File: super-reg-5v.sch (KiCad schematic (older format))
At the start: 41 parts, among them Q1 2SA1015, Q2 D44H11, U1 LM317T, U2 AD825, U3 AD825, X1 AC_IN, X2 DC_OUT

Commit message: migrate library
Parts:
- LED1: symbol LED -> LED-RESCUE-super-reg-5v
- U2, U3: symbol TL081 -> TL081-RESCUE-super-reg-5v
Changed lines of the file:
@@
 EESchema Schematic File Version 2
+LIBS:super-reg-5v-rescue
 LIBS:power
 LIBS:device
@@
 $EndComp
 $Comp
-L LED LED1
+L LED-RESCUE-super-reg-5v LED1
 U 1 1 57943EDE
 P 4700 3050
@@
 $EndComp
 $Comp
-L TL081 U2
+L TL081-RESCUE-super-reg-5v U2
 U 1 1 5794409D
 P 6900 3600
@@
 	3750 2350 4000 2350
 $Comp
-L TL081 U3
+L TL081-RESCUE-super-reg-5v U3
 U 1 1 57C2A197
 P 6900 4900

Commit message: update components
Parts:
- D3: symbol ZENER -> D_Zener
- JP1: symbol JUMPER3 -> Jumper_NC_Dual
- U2, U3: symbol TL081-RESCUE-super-reg-5v -> TL071
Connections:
- no-connect marks 0 -> 4
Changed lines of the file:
@@
 EESchema Schematic File Version 2
-LIBS:super-reg-5v-rescue
 LIBS:power
 LIBS:device
@@
 LIBS:DB-1
 LIBS:semi-trans-OnSemi
-LIBS:super-reg-5v-cache
 EELAYER 25 0
 EELAYER END
@@
 $EndComp
 $Comp
-L TL081-RESCUE-super-reg-5v U2
+L TL071 U2
 U 1 1 5794409D
 P 6900 3600
@@
 $EndComp
 $Comp
-L ZENER D3
+L D_Zener D3
 U 1 1 579441EA
 P 5800 3600
@@
 $EndComp
 $Comp
-L JUMPER3 JP1
+L Jumper_NC_Dual JP1
 U 1 1 5794546A
 P 6500 2450
@@
 	5100 3250 5100 3200
 Wire Wire Line
-	6000 3600 6050 3600
+	5950 3600 6050 3600
 Wire Wire Line
 	6350 3600 6600 3600
@@
 	5500 2850 5500 3900
 Wire Wire Line
-	5600 3600 5500 3600
+	5500 3600 5650 3600
 Connection ~ 5500 3600
 Wire Wire Line
@@
 	3750 2350 4000 2350
 $Comp
-L TL081-RESCUE-super-reg-5v U3
+L TL071 U3
 U 1 1 57C2A197
 P 6900 4900
@@
 	2950 5200 2400 5200
 Connection ~ 2400 5200
+NoConn ~ 6900 5200
+NoConn ~ 6800 5200
+NoConn ~ 6800 3900
+NoConn ~ 6900 3900
+$Comp
+L PWR_FLAG #PWR07
+U 1 1 591C8082
+P 6500 3000
+F 0 "#PWR07" H 6500 3000 50  0001 C CNN
+F 1 "PWR_FLAG" H 6500 3000 50  0001 C CNN
+F 2 "" H 6500 3000 60  0000 C CNN
+F 3 "" H 6500 3000 60  0000 C CNN
+	1    6500 3000
+	1    0    0    -1
+$EndComp
 $EndSCHEMATC

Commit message: fix library error
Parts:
- LED1: symbol LED-RESCUE-super-reg-5v -> LED
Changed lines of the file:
@@
 LIBS:DB-1
 LIBS:semi-trans-OnSemi
+LIBS:super-reg-5v-cache
 EELAYER 25 0
 EELAYER END
@@
 $EndComp
 $Comp
-L LED-RESCUE-super-reg-5v LED1
+L LED LED1
 U 1 1 57943EDE
 P 4700 3050
@@
 	6350 3600 6600 3600
 Wire Wire Line
-	4700 2700 4700 2850
+	4700 2700 4700 2900
 Wire Wire Line
 	4000 2700 5400 2700
@@
 	4800 3450 4700 3450
 Wire Wire Line
-	4700 3250 4700 3600
+	4700 3200 4700 3600
 Connection ~ 4700 3450
 Wire Wire Line

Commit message: update footprints
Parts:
- C11, C8: footprint Capacitors_ThroughHole:C_Radial_D8_L13_P3.8 -> Capacitors_ThroughHole:CP_Radial_D8.0mm_P3.80mm
- C3, C5, C6, C9: footprint Capacitors_ThroughHole:C_Radial_D6.3_L11.2_P2.5 -> Capacitors_ThroughHole:CP_Radial_D6.3mm_P2.50mm
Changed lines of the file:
@@
 F 0 "C3" H 4275 3550 50  0000 L CNN
 F 1 "100u 35v LowESR" H 4250 3650 50  0000 L CNN
-F 2 "Capacitors_ThroughHole:C_Radial_D6.3_L11.2_P2.5" H 4288 3300 50  0001 C CNN
+F 2 "Capacitors_ThroughHole:CP_Radial_D6.3mm_P2.50mm" H 4288 3300 50  0001 C CNN
 F 3 "" H 4250 3450 50  0000 C CNN
 	1    4250 3450
@@
 F 0 "C6" H 6125 2400 50  0000 L CNN
 F 1 "100u 35v LowESR" H 5350 2450 50  0000 L CNN
-F 2 "Capacitors_ThroughHole:C_Radial_D6.3_L11.2_P2.5" H 6138 2150 50  0001 C CNN
+F 2 "Capacitors_ThroughHole:CP_Radial_D6.3mm_P2.50mm" H 6138 2150 50  0001 C CNN
 F 3 "" H 6100 2300 50  0000 C CNN
 	1    6100 2300
@@
 F 0 "C5" H 5825 4000 50  0000 L CNN
 F 1 "100u LowESR" V 5650 3650 50  0000 L CNN
-F 2 "Capacitors_ThroughHole:C_Radial_D6.3_L11.2_P2.5" H 5838 3750 50  0001 C CNN
+F 2 "Capacitors_ThroughHole:CP_Radial_D6.3mm_P2.50mm" H 5838 3750 50  0001 C CNN
 F 3 "" H 5800 3900 50  0000 C CNN
 	1    5800 3900
@@
 F 0 "C8" H 7875 4050 50  0000 L CNN
 F 1 "100u EP-Cap" H 7500 3800 50  0000 L CNN
-F 2 "Capacitors_ThroughHole:C_Radial_D8_L13_P3.8" H 7888 3800 50  0001 C CNN
+F 2 "Capacitors_ThroughHole:CP_Radial_D8.0mm_P3.80mm" H 7888 3800 50  0001 C CNN
 F 3 "" H 7850 3950 50  0000 C CNN
 	1    7850 3950
@@
 F 0 "C9" H 9025 3600 50  0000 L CNN
 F 1 "100u" H 9025 3400 50  0000 L CNN
-F 2 "Capacitors_ThroughHole:C_Radial_D6.3_L11.2_P2.5" H 9038 3350 50  0001 C CNN
+F 2 "Capacitors_ThroughHole:CP_Radial_D6.3mm_P2.50mm" H 9038 3350 50  0001 C CNN
 F 3 "" H 9000 3500 50  0000 C CNN
 	1    9000 3500
@@
 F 0 "C11" H 9875 3650 50  0000 L CNN
 F 1 "220u OS-CON" H 9875 3450 50  0000 L CNN
-F 2 "Capacitors_ThroughHole:C_Radial_D8_L13_P3.8" H 9888 3400 50  0001 C CNN
+F 2 "Capacitors_ThroughHole:CP_Radial_D8.0mm_P3.80mm" H 9888 3400 50  0001 C CNN
 F 3 "" H 9850 3550 50  0000 C CNN
 	1    9850 3550

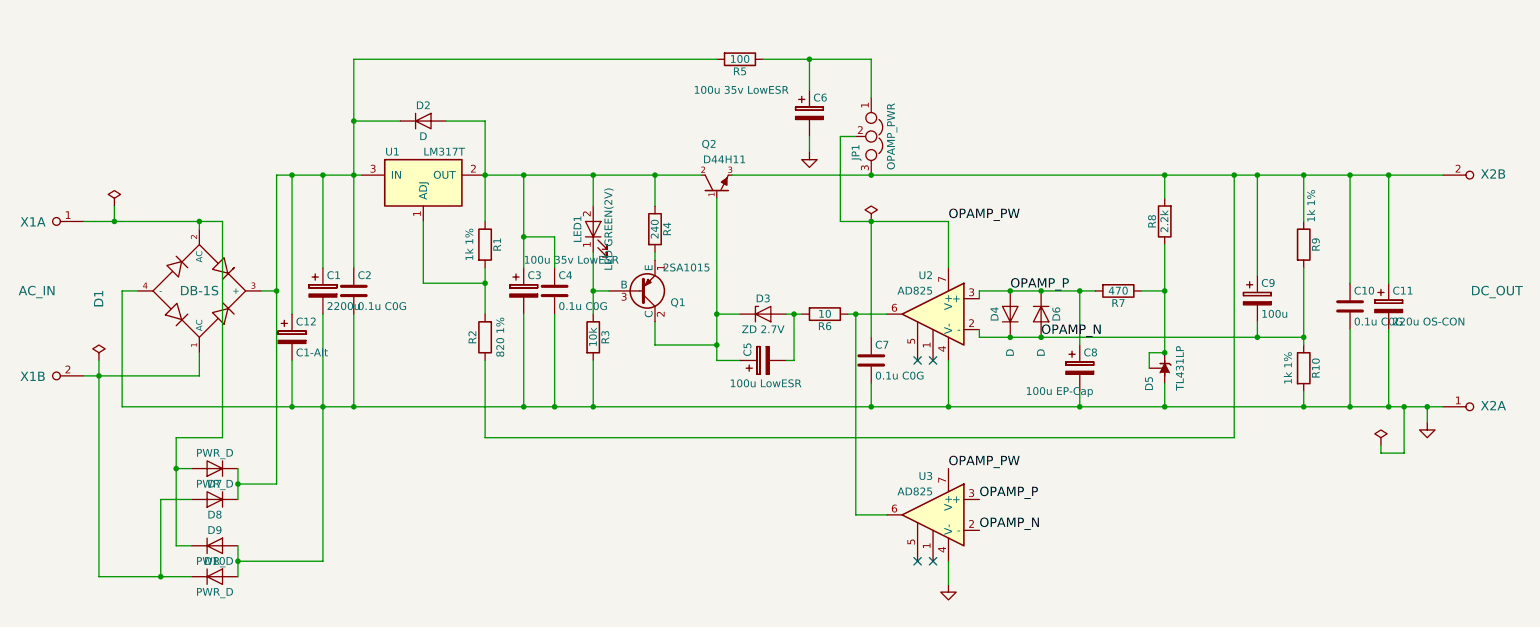
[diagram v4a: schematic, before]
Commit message: separate sensor input refactor components
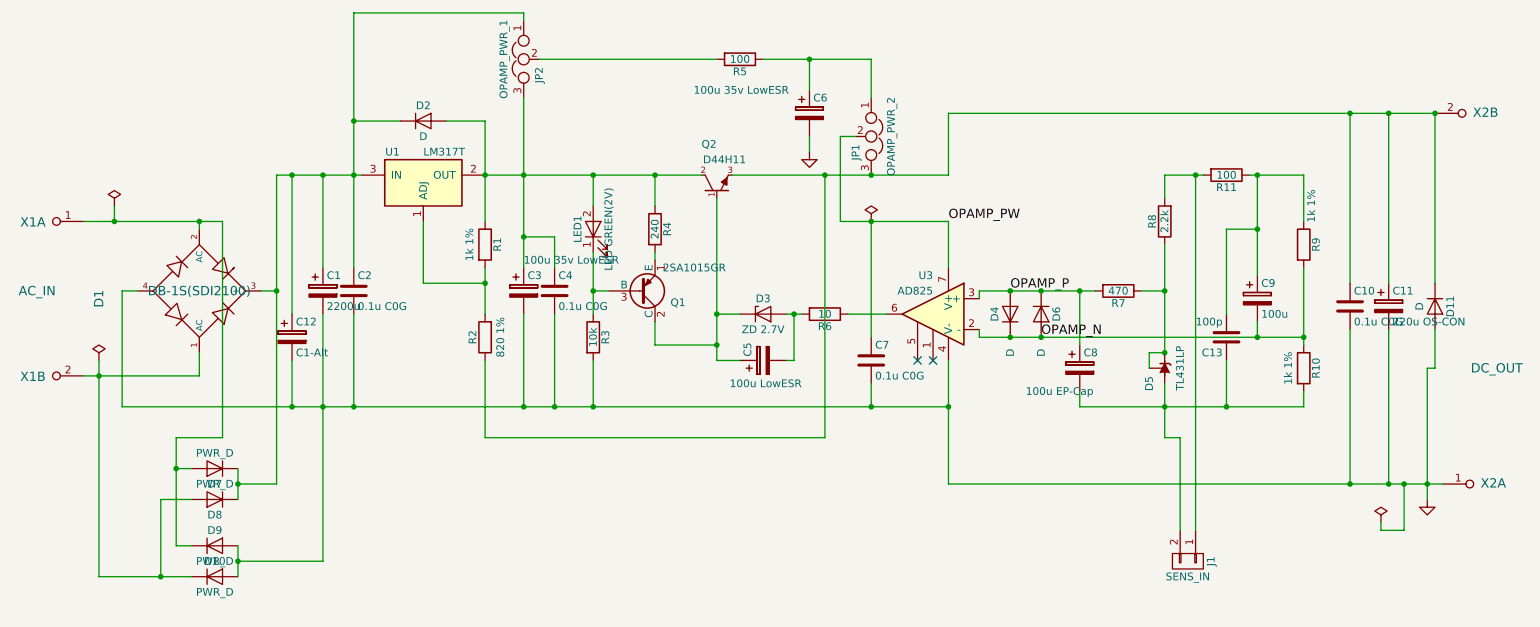
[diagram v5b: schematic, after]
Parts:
- removed U2: AD825, Housings_DIP:DIP-8_W7.62mm, symbol TL071
- added C13: 100p, Capacitors_SMD:C_0603_HandSoldering, symbol C
- added D11: D, Diodes_SMD:D_SMA_Handsoldering, symbol D
- added J1: SENS_IN, Connectors_JST:JST_XH_B02B-XH-A_02x2.50mm_Straight, symbol CONN_01X02
- added JP2: OPAMP_PWR_1, Connect:GS3, symbol Jumper_NC_Dual
- added R11: 100, Resistors_SMD:R_0603_HandSoldering, symbol R
- D1: value DB-1S -> DB-1S(SDI2100)
- D2: footprint Diodes_SMD:SMA_Handsoldering -> Diodes_SMD:D_SMA_Handsoldering
- JP1: value OPAMP_PWR -> OPAMP_PWR_2; footprint Pin_Headers:Pin_Header_Straight_1x03 -> Connect:GS3
- Q1: value 2SA1015 -> 2SA1015GR
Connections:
- net GND: now also D11.2 (A); no longer C8.2, D5.2 (A), R10.2
- net at C10.1, C11.1, JP1.3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: now also D11.1 (K); no longer C9.1, R8.2, R9.1
- net at C3.1, C4.1, D2.2 (A)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: now also JP2.3
- net at C1.1, C12.1, C2.1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: now also JP2.1; no longer R5.2
- new net: JP2.2, R5.2
- new net: J1.1 (P1), R11.2, R8.2
- new net: C13.1, C8.2, D5.2 (A), J1.2 (P2), R10.2
- new net: C13.2, C9.1, R11.1, R9.1
- no-connect marks 4 -> 2
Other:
- moved on the sheet: U3, X2A, X2B

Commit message: update transistor package changes for opams power
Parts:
- Q1: value 2SA1015GR -> 2SA1162GR; footprint TO_SOT_Packages_THT:TO-92_Inline_Wide -> TO_SOT_Packages_SMD:SC-59_Handsoldering; symbol 2SA1015 -> Q_PNP_BEC
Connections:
- net OPAMP_PW: now also C6.1, R5.1; no longer JP1.2
- net at Q1.1 (B): now also LED1.1 (K), R3.1; no longer R4.2
- net at C5.1, D3.1 (K), Q2.1 (B): now also Q1.3 (C); no longer Q1.2 (C)
- net at JP2.2: now also JP1.1; no longer R5.2
- new net: Q1.2 (E), R4.2
- new net: JP1.2, R5.2
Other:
- moved on the sheet: C6, R5
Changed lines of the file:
@@
 $EndComp
 $Comp
-L 2SA1015 Q1
+L Q_PNP_BEC Q1
 U 1 1 57943E83
 P 5000 3450
 F 0 "Q1" H 5200 3525 50  0000 L CNN
-F 1 "2SA1015GR" H 5150 3300 50  0000 L CNN
-F 2 "TO_SOT_Packages_THT:TO-92_Inline_Wide" H 4950 4500 50  0001 L CIN
+F 1 "2SA1162GR" H 5150 3300 50  0000 L CNN
+F 2 "TO_SOT_Packages_SMD:SC-59_Handsoldering" H 4950 4500 50  0001 L CIN
 F 3 "" H 5000 3450 50  0000 L CNN
 	1    5000 3450
@@
 L R R5
 U 1 1 57945578
-P 5650 1950
-F 0 "R5" V 5730 1950 50  0000 C CNN
-F 1 "100" V 5650 1950 50  0000 C CNN
-F 2 "Resistors_SMD:R_0805_HandSoldering" V 5580 1950 50  0001 C CNN
-F 3 "" H 5650 1950 50  0000 C CNN
-	1    5650 1950
-	0    1    1    0
+P 6150 2450
+F 0 "R5" V 6230 2450 50  0000 C CNN
+F 1 "100" V 6150 2450 50  0000 C CNN
+F 2 "Resistors_SMD:R_0805_HandSoldering" V 6080 2450 50  0001 C CNN
+F 3 "" H 6150 2450 50  0000 C CNN
+	1    6150 2450
+	0    -1   -1   0
 $EndComp
 $Comp
 L CP C6
 U 1 1 57945E44
-P 6100 2300
-F 0 "C6" H 6125 2400 50  0000 L CNN
-F 1 "100u 35v LowESR" H 5350 2450 50  0000 L CNN
-F 2 "Capacitors_ThroughHole:CP_Radial_D6.3mm_P2.50mm" H 6138 2150 50  0001 C CNN
-F 3 "" H 6100 2300 50  0000 C CNN
-	1    6100 2300
-	1    0    0    -1
-$EndComp
-$Comp
-L GND #PWR01
-U 1 1 57945ED5
-P 6100 2550
-F 0 "#PWR01" H 6100 2550 30  0001 C CNN
-F 1 "GND" H 6100 2480 30  0001 C CNN
-F 2 "" H 6100 2550 60  0000 C CNN
-F 3 "" H 6100 2550 60  0000 C CNN
-	1    6100 2550
+P 6400 3350
+F 0 "C6" H 6425 3450 50  0000 L CNN
+F 1 "100u 35v LowESR" H 5650 3500 50  0000 L CNN
+F 2 "Capacitors_ThroughHole:CP_Radial_D6.3mm_P2.50mm" H 6438 3200 50  0001 C CNN
+F 3 "" H 6400 3350 50  0000 C CNN
+	1    6400 3350
 	1    0    0    -1
 $EndComp
@@
 Connection ~ 6500 2700
 Wire Wire Line
-	6300 3000 7000 3000
-Wire Wire Line
-	6300 3000 6300 2450
-Wire Wire Line
-	6300 2450 6400 2450
+	6000 3000 7000 3000
 Wire Wire Line
 	6500 1950 6500 2200
 Wire Wire Line
-	5800 1950 6500 1950
-Wire Wire Line
-	6100 2550 6100 2450
-Wire Wire Line
-	6100 2150 6100 1950
-Connection ~ 6100 1950
+	4350 1950 6500 1950
 Wire Wire Line
 	6500 4200 6500 4050
@@
 Connection ~ 9600 2300
 Wire Wire Line
-	9850 3700 9850 4700
+	9850 4700 9850 3700
 Wire Wire Line
 	9600 3700 9600 4700
@@
 Connection ~ 10150 2300
 Wire Wire Line
-	5500 1950 4350 1950
-Wire Wire Line
 	4250 1650 3150 1650
 Connection ~ 3150 2350
@@
 	8800 3050 9000 3050
 Connection ~ 9000 3050
+Wire Wire Line
+	6300 2450 6400 2450
+Wire Wire Line
+	6400 3000 6400 3200
+Wire Wire Line
+	6000 3000 6000 2450
+Connection ~ 6400 3000
+Wire Wire Line
+	6400 3500 6400 4200
+Connection ~ 6400 4200
 $EndSCHEMATC

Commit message: for negative voltage
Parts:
- Q1: value 2SA1162GR -> 2SC2712GR; symbol Q_PNP_BEC -> Q_NPN_BEC
- Q2: value D44H11 -> D45H11; symbol D44H11 -> Q_PNP_BCE
- U1: value LM317T -> LM337T; symbol LM317T -> LM337_TO220
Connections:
- net OPAMP_N: now also C9.1; no longer C9.2
- net at C10.1, JP1.3, Q2.3 (E)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: now also C11.2, D11.2 (A); no longer C11.1, D11.1 (K)
- net at C4.1, JP2.3, Q2.2 (C)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: now also C3.2, D2.1 (K), LED1.1 (K), U1.3 (VO); no longer C3.1, D2.2 (A), LED1.2 (A), U1.2 (OUT)
- net at C1.1, C12.1, D1.3 (+)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: now also C10.2, C11.1, C2.2, C3.1, C4.2, C6.1, C7.2, D11.1 (K), R3.2, U3.7 (V+), X2.1; no longer C2.1, D2.1 (K), JP2.1, U1.3 (IN)
- net at Q1.1 (B), R3.1: now also LED1.2 (A); no longer LED1.1 (K)
- net at Q1.3 (C), Q2.1 (B): now also C5.2, D3.2 (A); no longer C5.1, D3.1 (K)
- net at R7.1, R8.1: now also D5.2 (A); no longer D5.1 (REF), D5.3 (K)
- net at R11.2, R8.2: now also J1.2 (P2); no longer J1.1 (P1)
- net at C13.2, R11.1, R9.1: now also C9.2; no longer C9.1
- net at D10.1 (K), D8.2 (A), X1.2: now also D1.2 (AC); no longer D1.1 (AC)
- net at D7.2 (A), D9.1 (K), X1.1: now also D1.1 (AC); no longer D1.2 (AC)
- removed net GND: C1.2, C10.2, C11.2, C12.2, C2.2, C3.2, C4.2, C6.2, C7.2, D1.4 (-), D10.2 (A), D11.2 (A), D9.2 (A), R3.2, U3.4 (V-), X2.1
- net OPAMP_P: no longer names the net of D4.2 (A), D6.1 (K), R7.2, U3.3 (+)
- net OPAMP_P: now also C8.2; no longer C8.1
- net OPAMP_PW: no longer names the net of C7.1, R5.1
- net OPAMP_PW: now also C6.2, U3.4 (V-); no longer C6.1, U3.7 (V+)
- new net: C1.2, C12.2, C2.1, D1.4 (-), D10.2 (A), D2.2 (A), D9.2 (A), JP2.1, U1.2 (VI)
- new net: C5.1, D3.1 (K), R6.2
- new net: C13.1, C8.1, D5.1 (REF), D5.3 (K), J1.1 (P1), R10.2
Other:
- moved on the sheet: D5, LED1, U1

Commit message: update values
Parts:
- D3: value ZD 2.7V -> ZD 6.8V
- R8: value 2.2k -> 4.7k
- R9: value 1k 1% -> 1.5k 1%
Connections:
- net at C1.1, C10.2, C11.1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: no longer C12.1
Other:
- note added: "Default: JP1, 3 to 2"
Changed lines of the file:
@@
-EESchema Schematic File Version 2
-LIBS:power
-LIBS:device
-LIBS:transistors
-LIBS:conn
-LIBS:linear
-LIBS:regul
-LIBS:74xx
-LIBS:cmos4000
-LIBS:adc-dac
-LIBS:memory
-LIBS:xilinx
-LIBS:microcontrollers
-LIBS:dsp
-LIBS:microchip
-LIBS:analog_switches
-LIBS:motorola
-LIBS:texas
-LIBS:intel
-LIBS:audio
-LIBS:interface
-LIBS:digital-audio
-LIBS:philips
-LIBS:display
-LIBS:cypress
-LIBS:siliconi
-LIBS:opto
-LIBS:atmel
-LIBS:contrib
-LIBS:valves
-LIBS:references
-LIBS:ab2_terminal_block
-LIBS:DB-1
-LIBS:semi-trans-OnSemi
-LIBS:super-reg-5v-cache
-EELAYER 25 0
+EESchema Schematic File Version 4
+EELAYER 30 0
 EELAYER END
 $Descr A4 11693 8268
@@
 P 5800 3600
 F 0 "D3" H 5800 3700 50  0000 C CNN
-F 1 "ZD 2.7V" H 5800 3500 50  0000 C CNN
+F 1 "ZD 6.8V" H 5800 3500 50  0000 C CNN
 F 2 "Diodes_ThroughHole:Diode_DO-35_SOD27_Horizontal_RM10" H 5800 3600 50  0001 C CNN
 F 3 "" H 5800 3600 50  0000 C CNN
@@
 P 8400 3000
 F 0 "R8" V 8480 3000 50  0000 C CNN
-F 1 "2.2k" V 8400 3000 50  0000 C CNN
+F 1 "4.7k" V 8400 3000 50  0000 C CNN
 F 2 "Resistors_SMD:R_0603_HandSoldering" V 8330 3000 50  0001 C CNN
 F 3 "" H 8400 3000 50  0000 C CNN
@@
 P 9300 3150
 F 0 "R9" V 9380 3150 50  0000 C CNN
-F 1 "1k 1%" V 9350 3400 50  0000 C CNN
+F 1 "1.5k 1%" V 9350 3400 50  0000 C CNN
 F 2 "Resistors_SMD:R_0603_HandSoldering" V 9230 3150 50  0001 C CNN
 F 3 "" H 9300 3150 50  0000 C CNN
@@
 	5100 3250 5100 3200
 Wire Wire Line
-	5950 3600 6050 3600
+	5950 3600 6000 3600
 Wire Wire Line
 	6350 3600 6600 3600
@@
 	4700 2700 4700 2900
 Wire Wire Line
-	3900 2700 5300 2700
+	3900 2700 4000 2700
 Wire Wire Line
 	5100 2700 5100 2900
@@
 	4800 3450 4700 3450
 Wire Wire Line
-	4700 3200 4700 3600
+	4700 3200 4700 3450
 Connection ~ 4700 3450
 Wire Wire Line
@@
 	5500 3800 5100 3800
 Wire Wire Line
-	5500 3000 5500 3900
+	5500 3000 5500 3600
 Wire Wire Line
 	5500 3600 5650 3600
 Wire Wire Line
-	4000 2350 4000 3000
+	4000 2350 4000 2700
 Connection ~ 4700 2700
 Connection ~ 4000 2700
@@
 	3600 3400 4000 3400
 Wire Wire Line
-	4000 3300 4000 3600
+	4000 3300 4000 3400
 Connection ~ 4000 3400
 Wire Wire Line
-	4250 2200 4250 3300
+	4250 2200 4250 2700
 Connection ~ 4250 2700
 Wire Wire Line
@@
 Connection ~ 4450 4200
 Wire Wire Line
-	1750 2700 3300 2700
-Wire Wire Line
-	3150 1650 3150 3300
+	1750 2700 2750 2700
+Wire Wire Line
+	3150 1650 3150 2350
 Wire Wire Line
 	2950 3300 2950 2700
@@
 Connection ~ 6500 2700
 Wire Wire Line
-	6000 3000 6850 3000
+	6000 3000 6400 3000
 Wire Wire Line
 	6500 1950 6500 2200
@@
 Connection ~ 6500 3000
 Wire Wire Line
-	7300 3750 9300 3750
-Wire Wire Line
-	7300 3450 7950 3450
+	7300 3750 7400 3750
+Wire Wire Line
+	7300 3450 7400 3450
 Wire Wire Line
 	5500 3900 5650 3900
@@
 	8400 2700 8400 2850
 Wire Wire Line
-	9000 2700 9000 3350
+	9000 2700 9000 3050
 Wire Wire Line
 	9000 3750 9000 3650
 Connection ~ 7600 3750
 Wire Wire Line
-	8400 4050 8400 4400
-Wire Wire Line
-	9300 3300 9300 3800
+	8400 4050 8400 4100
+Wire Wire Line
+	9300 3300 9300 3750
 Connection ~ 9000 3750
 Connection ~ 9300 3750
@@
 	9300 2700 9300 3000
 Wire Wire Line
-	7000 2300 10150 2300
+	7000 2300 9600 2300
 Wire Wire Line
 	9600 2300 9600 3400
@@
 Connection ~ 9850 4700
 Wire Wire Line
-	1400 4000 2300 4000
+	1400 4000 1500 4000
 Connection ~ 2950 4200
 Wire Wire Line
 	2550 3450 2650 3450
 Wire Wire Line
-	2650 3450 2650 4700
+	2650 3450 2650 4200
 Connection ~ 2950 2700
 Wire Wire Line
@@
 Connection ~ 9000 2700
 Wire Wire Line
-	8400 3150 8400 3850
-Wire Wire Line
-	1500 3900 1500 5300
+	8400 3150 8400 3450
+Wire Wire Line
+	1500 3900 1500 4000
 Connection ~ 1500 4000
 Wire Wire Line
-	1600 2900 1600 3850
+	1600 2900 1600 3000
 Connection ~ 10100 4700
 Connection ~ 9850 2300
@@
 	2750 3900 2750 4200
 Wire Wire Line
-	2400 4600 2400 4800
+	2400 4600 2400 4700
 Wire Wire Line
 	2650 4700 2400 4700
@@
 	2100 4600 2000 4600
 Wire Wire Line
-	2000 3850 2000 5100
+	2000 3850 2000 4600
 Wire Wire Line
 	2000 5100 2100 5100
@@
 	1900 4800 1900 5300
 Wire Wire Line
-	1500 5300 2100 5300
+	1500 5300 1900 5300
 Connection ~ 1900 5300
 Wire Wire Line
@@
 	4250 1700 4250 1650
 Wire Wire Line
-	2750 4200 7000 4200
-Wire Wire Line
-	7850 4200 9300 4200
-Wire Wire Line
-	7000 4700 10200 4700
-Wire Wire Line
-	5700 2700 7000 2700
+	7850 4200 8400 4200
+Wire Wire Line
+	7000 4700 9600 4700
+Wire Wire Line
+	5700 2700 6200 2700
 Wire Wire Line
 	7000 2700 7000 2300
@@
 	6200 4400 6200 2700
 Wire Wire Line
-	8950 2700 9300 2700
+	8950 2700 9000 2700
 Wire Wire Line
 	8500 5000 8500 4400
@@
 	8500 4400 8400 4400
 Wire Wire Line
-	8400 2700 8650 2700
+	8400 2700 8600 2700
 Wire Wire Line
 	8600 2700 8600 5000
@@
 Wire Wire Line
 	3900 2700 3900 2750
-Wire Wire Line
-	2800 4200 2650 4200
 Connection ~ 2650 4200
-Connection ~ 2800 4200
-Wire Wire Line
-	1750 2700 1750 5550
+Wire Wire Line
+	1750 2700 1750 3450
 Connection ~ 2750 2700
 Wire Wire Line
@@
 Connection ~ 5100 2700
 Wire Wire Line
-	1600 3850 2150 3850
+	1600 3850 2000 3850
 Connection ~ 2000 4600
 Connection ~ 2000 3850
@@
 	7300 3500 7200 3500
 Connection ~ 7400 3450
+Wire Wire Line
+	4700 3450 4700 3600
+Wire Wire Line
+	4700 2700 5100 2700
+Wire Wire Line
+	4000 2700 4250 2700
+Wire Wire Line
+	4000 2700 4000 3000
+Wire Wire Line
+	4000 3400 4000 3600
+Wire Wire Line
+	4250 2700 4250 3100
+Wire Wire Line
+	4250 2700 4700 2700
+Wire Wire Line
+	4250 3100 4250 3300
+Wire Wire Line
+	4700 4200 6400 4200
+Wire Wire Line
+	4450 4200 4700 4200
+Wire Wire Line
+	3150 2700 3300 2700
+Wire Wire Line
+	3150 2700 3150 3300
+Wire Wire Line
+	4250 4200 4450 4200
+Wire Wire Line
+	3150 4200 4250 4200
+Wire Wire Line
+	6500 2700 7000 2700
+Wire Wire Line
+	6500 4200 6700 4200
+Wire Wire Line
+	6500 3000 6850 3000
+Wire Wire Line
+	5500 3800 5500 3900
+Wire Wire Line
+	6000 3600 6050 3600
+Wire Wire Line
+	7600 3450 7850 3450
+Wire Wire Line
+	7850 3450 7950 3450
+Wire Wire Line
+	8400 3450 8400 3850
+Wire Wire Line
+	7600 3750 9000 3750
+Wire Wire Line
+	9000 3750 9300 3750
+Wire Wire Line
+	9300 3750 9300 3800
+Wire Wire Line
+	8400 4200 8400 4400
+Wire Wire Line
+	8400 4200 8800 4200
+Wire Wire Line
+	9600 2300 9850 2300
+Wire Wire Line
+	9600 4700 9850 4700
+Wire Wire Line
+	9850 4700 9950 4700
+Wire Wire Line
+	2950 4200 3150 4200
+Wire Wire Line
+	2950 2700 3150 2700
+Wire Wire Line
+	9950 4700 10100 4700
+Wire Wire Line
+	9000 2700 9300 2700
+Wire Wire Line
+	1500 4000 2300 4000
+Wire Wire Line
+	1500 4000 1500 5300
+Wire Wire Line
+	10100 4700 10200 4700
+Wire Wire Line
+	9850 2300 10150 2300
+Wire Wire Line
+	2400 4700 2400 4800
+Wire Wire Line
+	1900 5300 2100 5300
+Wire Wire Line
+	3150 2350 3150 2700
+Wire Wire Line
+	8600 2700 8650 2700
+Wire Wire Line
+	8800 4200 9300 4200
+Wire Wire Line
+	9000 3050 9000 3350
+Wire Wire Line
+	6400 3000 6500 3000
+Wire Wire Line
+	6400 4200 6500 4200
+Wire Wire Line
+	2650 4200 2650 4700
+Wire Wire Line
+	2750 2700 2950 2700
+Wire Wire Line
+	1750 3450 1750 5550
+Wire Wire Line
+	6700 4200 7000 4200
+Wire Wire Line
+	8400 4100 8400 4200
+Wire Wire Line
+	5500 3600 5500 3800
+Wire Wire Line
+	6200 2700 6500 2700
+Wire Wire Line
+	5100 2700 5300 2700
+Wire Wire Line
+	2000 4600 2000 5100
+Wire Wire Line
+	2000 3850 2150 3850
+Wire Wire Line
+	1600 3000 1600 3850
+Wire Wire Line
+	7400 3750 7600 3750
+Wire Wire Line
+	7400 3450 7600 3450
+Wire Wire Line
+	2650 4200 2950 4200
+Text Notes 6450 2850 0    60   ~ 0
+Default: JP1, 3 to 2
 $EndSCHEMATC
